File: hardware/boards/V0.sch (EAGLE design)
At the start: 134 parts, among them IC2 TPS6300, J1 SJ-43515TS-SMT, J2 HIROSE_DM3BT-DSF-PEJSHIROSE_D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, J3 MOLEX_105450-0101MOLEX_105450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, Q2 ON_SEMI_MMBT5551LT1GON_SEMI_M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, U1 VS1053-L, U2 MICROCHIP_MCP73831T-2ATI-OTMI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, X3 FH12-45S-0.5SH

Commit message: schematic: done!?
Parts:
- R31: value 1k -> 2k
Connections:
- removed net BLUE_LED_CATH: D1.BLUE_CATHODE
- removed net IO18: R8.1, U$1.IO18
- removed net N$42: U1G$1.SO
- removed net N$43: U1G$1.SI
- removed net N$44: U1G$1.SCLK
- removed net N$45: U1G$1.XCS
- removed net N$46: U1G$1.XDCS/BSYNC
- removed net N$47: U1G$1.DREQ
- new net DREQ: U$1.IO26, U1G$1.DREQ
- new net SPI_MISO: U$1.IO19, U1G$1.SO, X3-29.1
- new net VIB_MOTOR: R8.1, U$1.IO10
- new net VS_CMD_CS: U$1.IO27, U1G$1.XCS
- new net VS_DATA_CS: U$1.IO5, U1G$1.XDCS/BSYNC
- net ATQ_CHANGE: now also U$1.IO25
- net BUTTON_ADC: now also U$1.IO34
- net BUTTON_DIN: now also U$1.SENSOR_VN
- net CP_VDD: no longer C24.+, C25.+, R31.2
- net DISPLAY_CS: now also U$1.IO32
- net DISPLAY_RST: now also U$1.IO33
- net GND: now also J2.MNT_2, J2.MNT_3, J2.MNT_4, X3-3.1; no longer X3-31.1, X3-33.1
- net GREEN_LED_CATH: now also U$1.IO9
- net I2C_SCL: now also U$1.IO22
- net I2C_SDA: now also U$1.IO21
- net IO0: now also D1.BLUE_CATHODE
- net IO12: now also U$1.IO12
- net IO13: now also U$1.IO13
- net IO14: now also R7.2, U$1.IO14; no longer R6.2
- net IO15: now also R6.2, U$1.IO15; no longer R7.2
- net IO2: now also U$1.IO2
- net IO4: now also U$1.IO4
- net SPI_CLK: now also U$1.IO18, U1G$1.SCLK
- net SPI_MOSI: now also U$1.IO23, U1G$1.SI
- net V3P3: now also C24.+, C25.+, R31.2, X3-31.1, X3-33.1
- net VBAT_ADC_IN: now also U$1.SENSOR_CAPN
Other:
- moved on the sheet: R44

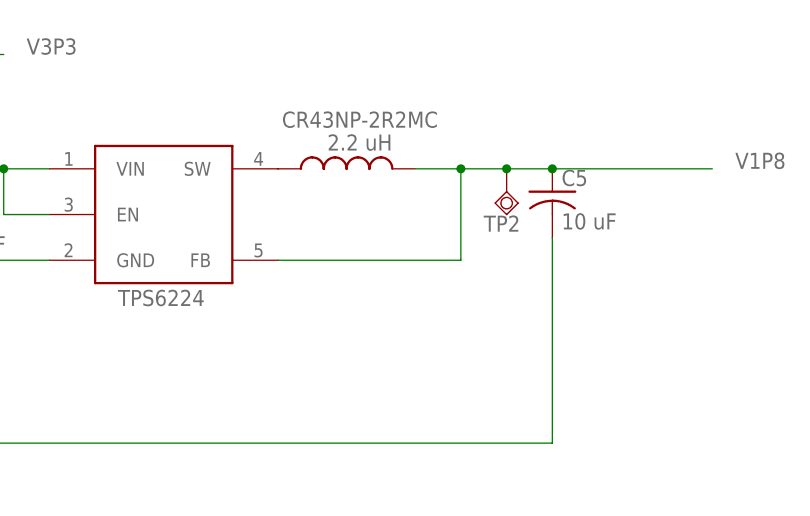
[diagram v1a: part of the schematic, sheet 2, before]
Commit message: minor fixes: this is an adjustable 1.8V regulator..
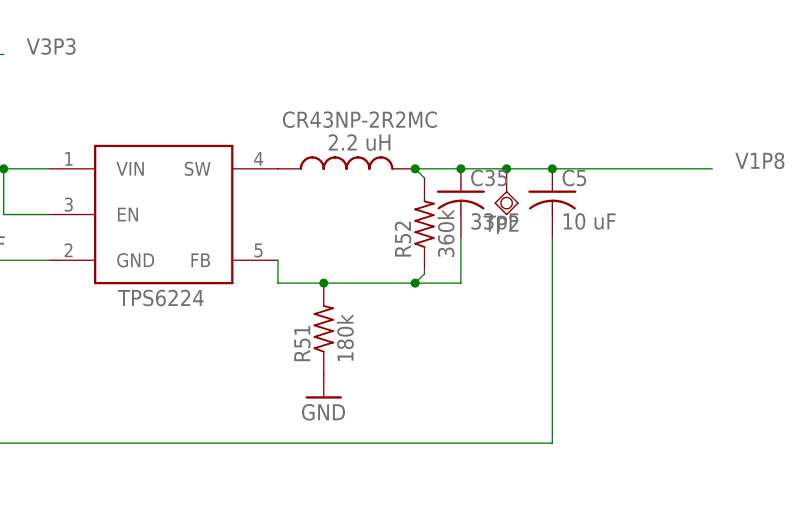
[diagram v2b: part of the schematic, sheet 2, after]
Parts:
- added C35: 33pF, rcl:C-USC0805
- added R51: 180k, rcl:R-US_R0805
- added R52: 360k, rcl:R-US_R0805
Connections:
- new net N$42: C35.2, R51.2, R52.1, TPS6224.FB
- net GND: now also R51.1
- net V1P8: now also C35.1, R52.2; no longer TPS6224.FB
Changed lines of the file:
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@@
 <setting verticaltext="up"/>
 </settings>
-<grid distance="0.1" unitdist="inch" unit="inch" style="lines" multiple="1" display="no" altdistance="0.01" altunitdist="inch" altunit="inch"/>
+<grid distance="0.1" unitdist="inch" unit="inch" style="lines" multiple="1" display="no" altdistance="0.000000123031" altunitdist="inch" altunit="inch"/>
 <layers>
 <layer number="1" name="Top" color="4" fill="1" visible="no" active="no"/>
@@
 <part name="GND44" library="supply1" library_urn="urn:adsk.eagle:library:371" deviceset="GND" device=""/>
 <part name="GND45" library="supply1" library_urn="urn:adsk.eagle:library:371" deviceset="GND" device=""/>
+<part name="C35" library="rcl" library_urn="urn:adsk.eagle:library:334" deviceset="C-US" device="C0805" package3d_urn="urn:adsk.eagle:package:23617/2" value="33pF"/>
+<part name="R51" library="rcl" library_urn="urn:adsk.eagle:library:334" deviceset="R-US_" device="R0805" package3d_urn="urn:adsk.eagle:package:23553/2" value="180k"/>
+<part name="R52" library="rcl" library_urn="urn:adsk.eagle:library:334" deviceset="R-US_" device="R0805" package3d_urn="urn:adsk.eagle:package:23553/2" value="360k"/>
+<part name="GND46" library="supply1" library_urn="urn:adsk.eagle:library:371" deviceset="GND" device=""/>
 </parts>
 <sheets>
@@
 <attribute name="TP_SIGNAL_NAME" x="76.2" y="3.81" size="1.778" layer="97"/>
 </instance>
+<instance part="C35" gate="G$1" x="68.58" y="5.08" smashed="yes">
+<attribute name="NAME" x="69.596" y="5.715" size="1.778" layer="95"/>
+<attribute name="VALUE" x="69.596" y="0.889" size="1.778" layer="96"/>
+</instance>
+<instance part="R51" gate="G$1" x="53.34" y="-10.16" smashed="yes" rot="R90">
+<attribute name="NAME" x="51.8414" y="-13.97" size="1.778" layer="95" rot="R90"/>
+<attribute name="VALUE" x="56.642" y="-13.97" size="1.778" layer="96" rot="R90"/>
+</instance>
+<instance part="R52" gate="G$1" x="64.534971875" y="1.4628125" smashed="yes" rot="R90">
+<attribute name="NAME" x="63.036371875" y="-2.3471875" size="1.778" layer="95" rot="R90"/>
+<attribute name="VALUE" x="67.836971875" y="-2.3471875" size="1.778" layer="96" rot="R90"/>
+</instance>
+<instance part="GND46" gate="1" x="53.34" y="-17.78" smashed="yes">
+<attribute name="VALUE" x="50.8" y="-20.32" size="1.778" layer="96"/>
+</instance>
 </instances>
 <busses>
@@
 <wire x1="-101.6" y1="48.26" x2="-101.6" y2="50.8" width="0.1524" layer="91"/>
 </segment>
+<segment>
+<pinref part="R51" gate="G$1" pin="1"/>
+<pinref part="GND46" gate="1" pin="GND"/>
+</segment>
 </net>
 <net name="V1P8" class="0">
 <segment>
-<pinref part="TPS6224" gate="G$1" pin="FB"/>
-<wire x1="48.26" y1="-2.54" x2="68.58" y2="-2.54" width="0.1524" layer="91"/>
-<wire x1="68.58" y1="-2.54" x2="68.58" y2="7.62" width="0.1524" layer="91"/>
-<wire x1="68.58" y1="7.62" x2="63.5" y2="7.62" width="0.1524" layer="91"/>
 <pinref part="U$5" gate="G$1" pin="2"/>
 <pinref part="TP2" gate="G$1" pin="TP"/>
+<wire x1="63.5" y1="7.62" x2="68.58" y2="7.62" width="0.1524" layer="91"/>
+<pinref part="C5" gate="G$1" pin="1"/>
 <wire x1="68.58" y1="7.62" x2="73.66" y2="7.62" width="0.1524" layer="91"/>
-<junction x="68.58" y="7.62"/>
-<pinref part="C5" gate="G$1" pin="1"/>
 <wire x1="78.74" y1="7.62" x2="96.52" y2="7.62" width="0.1524" layer="91"/>
 <label x="99.06" y="7.62" size="1.778" layer="95"/>
@@
 <junction x="73.66" y="7.62"/>
 <junction x="78.74" y="7.62"/>
+<pinref part="C35" gate="G$1" pin="1"/>
+<junction x="68.58" y="7.62"/>
+<pinref part="R52" gate="G$1" pin="2"/>
+<wire x1="64.534971875" y1="6.5428125" x2="64.534971875" y2="6.585028125" width="0.1524" layer="91"/>
+<wire x1="64.534971875" y1="6.585028125" x2="63.5" y2="7.62" width="0.1524" layer="91"/>
+<junction x="63.5" y="7.62"/>
 </segment>
 </net>
@@
 </segment>
 </net>
+<net name="N$42" class="0">
+<segment>
+<pinref part="TPS6224" gate="G$1" pin="FB"/>
+<wire x1="48.26" y1="-2.54" x2="48.26" y2="-5.08" width="0.1524" layer="91"/>
+<pinref part="R51" gate="G$1" pin="2"/>
+<wire x1="48.26" y1="-5.08" x2="53.34" y2="-5.08" width="0.1524" layer="91"/>
+<wire x1="53.34" y1="-5.08" x2="63.5" y2="-5.08" width="0.1524" layer="91"/>
+<junction x="53.34" y="-5.08"/>
+<pinref part="C35" gate="G$1" pin="2"/>
+<wire x1="63.5" y1="-5.08" x2="68.58" y2="-5.08" width="0.1524" layer="91"/>
+<wire x1="68.58" y1="-5.08" x2="68.58" y2="0" width="0.1524" layer="91"/>
+<pinref part="R52" gate="G$1" pin="1"/>
+<wire x1="64.534971875" y1="-3.6171875" x2="64.534971875" y2="-4.045028125" width="0.1524" layer="91"/>
+<wire x1="64.534971875" y1="-4.045028125" x2="63.5" y2="-5.08" width="0.1524" layer="91"/>
+<junction x="63.5" y="-5.08"/>
+</segment>
+</net>

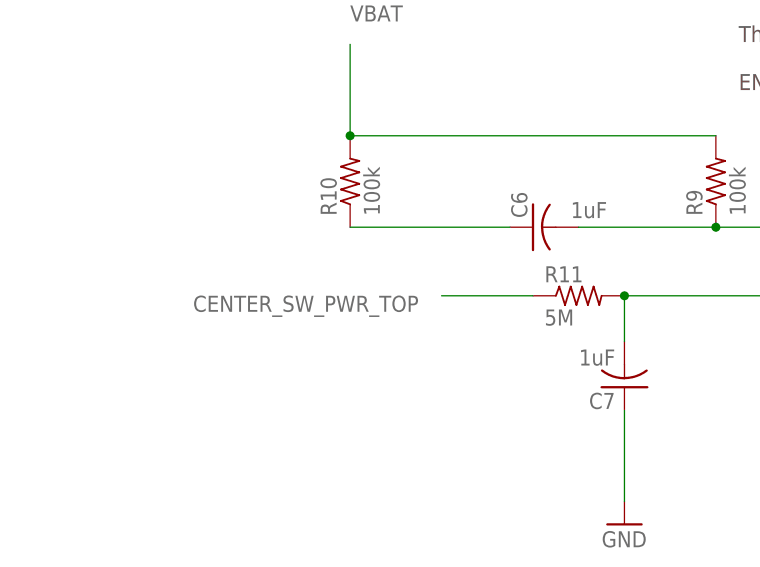
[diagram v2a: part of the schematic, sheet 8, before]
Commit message: Power on/off changes + misc fixes
Corrected the power on/off circuit (connected the top of the switch to the right net) and bumped up the resistor value so that it'll take ~6 seconds of the power button being held down to power off.
The circuit should now match Figure 5 from [this](http://www.mosaic-industries.com/embedded-systems/microcontroller-projects/electronic-circuits/push-button-switch-turn-on/latching-toggle-power-switch).

This fixes #1.

Additionally, libraries used in the V0 files should match the rearranged folders.
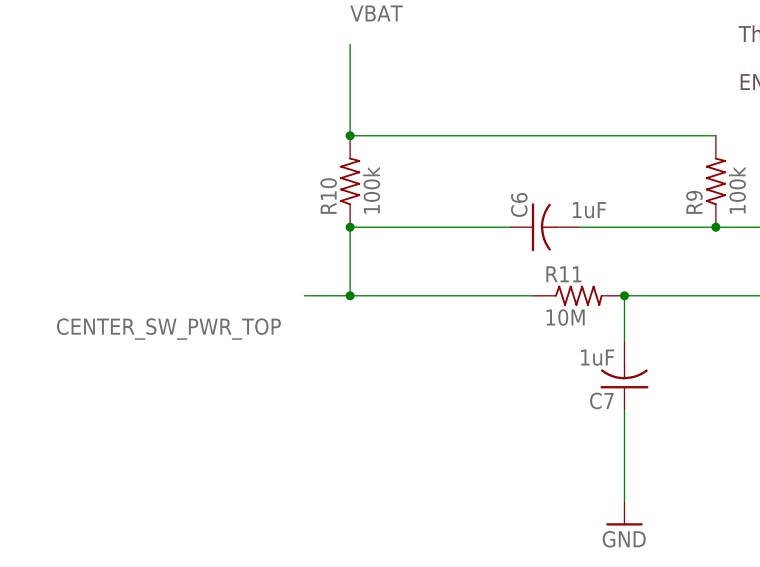
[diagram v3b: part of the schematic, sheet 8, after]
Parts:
- R11: value 5M -> 10M
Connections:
- removed net CENTER_SW_PWR_BTM: CENTER_SW_PWR.4
- removed net N$12: C6.1, R10.1
- net CENTER_SW_PWR_TOP: now also C6.1, R10.1
- net GND: now also CENTER_SW_PWR.4
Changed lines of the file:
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@@
 <setting verticaltext="up"/>
 </settings>
-<grid distance="0.1" unitdist="inch" unit="inch" style="lines" multiple="1" display="no" altdistance="0.000000123031" altunitdist="inch" altunit="inch"/>
+<grid distance="0.1" unitdist="inch" unit="inch" style="lines" multiple="1" display="no" altdistance="0.01" altunitdist="inch" altunit="inch"/>
 <layers>
 <layer number="1" name="Top" color="4" fill="1" visible="no" active="no"/>
@@
 <part name="C7" library="rcl" library_urn="urn:adsk.eagle:library:334" deviceset="C-US" device="C1206" package3d_urn="urn:adsk.eagle:package:23618/2" value="1uF"/>
 <part name="U$2" library="TOSHIBA_NAND-GATE" deviceset="TOSHIBA-NAND-GATE" device=""/>
-<part name="R11" library="rcl" library_urn="urn:adsk.eagle:library:334" deviceset="R-US_" device="R0805" package3d_urn="urn:adsk.eagle:package:23553/2" value="5M"/>
+<part name="R11" library="rcl" library_urn="urn:adsk.eagle:library:334" deviceset="R-US_" device="R0805" package3d_urn="urn:adsk.eagle:package:23553/2" value="10M"/>
 <part name="GND22" library="supply1" library_urn="urn:adsk.eagle:library:371" deviceset="GND" device=""/>
 <part name="X3" library="con-hirose" library_urn="urn:adsk.eagle:library:152" deviceset="FH12-45S-0.5S" device="H" package3d_urn="urn:adsk.eagle:package:7301/1"/>
@@
 </segment>
 </net>
-<net name="N$12" class="0">
-<segment>
-<pinref part="R10" gate="G$1" pin="1"/>
-<pinref part="C6" gate="G$1" pin="1"/>
-<wire x1="-43.18" y1="22.86" x2="-25.4" y2="22.86" width="0.1524" layer="91"/>
-</segment>
-</net>
 <net name="N$14" class="0">
 <segment>
@@
 <segment>
 <pinref part="R11" gate="G$1" pin="1"/>
-<wire x1="-22.86" y1="15.24" x2="-33.02" y2="15.24" width="0.1524" layer="91"/>
-<label x="-35.56" y="15.24" size="1.778" layer="95" rot="R180"/>
+<label x="-50.8" y="12.7" size="1.778" layer="95" rot="R180"/>
+<pinref part="R10" gate="G$1" pin="1"/>
+<pinref part="C6" gate="G$1" pin="1"/>
+<wire x1="-43.18" y1="22.86" x2="-25.4" y2="22.86" width="0.1524" layer="91"/>
+<wire x1="-43.18" y1="22.86" x2="-43.18" y2="15.24" width="0.1524" layer="91"/>
+<junction x="-43.18" y="22.86"/>
+<wire x1="-43.18" y1="15.24" x2="-22.86" y2="15.24" width="0.1524" layer="91"/>
+<wire x1="-43.18" y1="15.24" x2="-48.26" y2="15.24" width="0.1524" layer="91"/>
+<junction x="-43.18" y="15.24"/>
 </segment>
 </net>
@@
 <pinref part="GND7" gate="1" pin="GND"/>
 </segment>
+<segment>
+<pinref part="CENTER_SW_PWR" gate="G$0" pin="4"/>
+<pinref part="GND31" gate="1" pin="GND"/>
+<wire x1="139.7" y1="17.78" x2="139.7" y2="10.16" width="0.1524" layer="91"/>
+</segment>
 </net>
 <net name="BUTTON_DIN" class="0">
@@
 </segment>
 </net>
-<net name="CENTER_SW_PWR_BTM" class="0">
-<segment>
-<pinref part="CENTER_SW_PWR" gate="G$0" pin="4"/>
-<wire x1="139.7" y1="17.78" x2="139.7" y2="10.16" width="0.1524" layer="91"/>
-<pinref part="GND31" gate="1" pin="GND"/>
-<wire x1="139.7" y1="17.78" x2="170.18" y2="17.78" width="0.1524" layer="91"/>
-<junction x="139.7" y="17.78"/>
-<label x="170.18" y="17.78" size="1.778" layer="95"/>
-</segment>
-</net>
